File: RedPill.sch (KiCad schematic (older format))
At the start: 43 parts, among them J1 Conn_01x20, J2 Conn_01x20, J3 USB_C_Receptacle_USB2.0, J4 TagConnect_TC2030_SWD, J5 Conn_01x04, J6 Micro_SD_Card, SW1 SW_Push, U1 STM32F722RETx, U2 SRV05-4, U3 XC6206PxxxMR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

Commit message: Finish layout
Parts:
- added C?: 100nF, Capacitor_SMD:C_0402_1005Metric, symbol Device:C
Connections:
- net +3V3: now also C?.2
- net D+: now also U2.1 (IO1); no longer U2.3 (IO2)
- net D-: now also U2.3 (IO2); no longer U2.1 (IO1)
- net GND: now also C?.1
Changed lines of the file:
@@
 	1600 1350 1650 1350
 Wire Wire Line
-	1650 1350 1650 1400
-Wire Wire Line
 	1650 1450 1600 1450
 Wire Wire Line
 	1600 1550 1650 1550
-Wire Wire Line
-	1650 1550 1650 1600
 Wire Wire Line
 	1650 1650 1600 1650
@@
 Wire Wire Line
 	2050 1100 2050 1200
-Wire Wire Line
-	2250 1400 1650 1400
-Connection ~ 1650 1400
-Wire Wire Line
-	1650 1400 1650 1450
-Wire Wire Line
-	2250 1600 1650 1600
-Connection ~ 1650 1600
-Wire Wire Line
-	1650 1600 1650 1650
 NoConn ~ 1600 1950
 NoConn ~ 1600 2050
@@
 Text Label 1950 1400 0    50   ~ 0
 D-
-Text Label 1950 1600 0    50   ~ 0
+Text Label 1750 1600 0    50   ~ 0
 D+
 $Comp
@@
 	5100 3250 4950 3250
 Wire Wire Line
-	4950 3250 4950 2100
+	4950 3250 4950 2400
 $Comp
 L power:+3V3 #PWR0120
@@
 Wire Wire Line
 	2150 4550 5100 4550
+Wire Wire Line
+	1650 1350 1650 1400
+Wire Wire Line
+	1650 1550 1650 1600
+Wire Wire Line
+	1650 1600 2100 1600
+Wire Wire Line
+	2100 1600 2100 1400
+Wire Wire Line
+	2100 1400 2250 1400
+Connection ~ 1650 1600
+Wire Wire Line
+	1650 1600 1650 1650
+Wire Wire Line
+	1650 1400 2050 1400
+Wire Wire Line
+	2050 1400 2050 1500
+Wire Wire Line
+	2050 1500 2150 1500
+Wire Wire Line
+	2150 1500 2150 1600
+Wire Wire Line
+	2150 1600 2250 1600
+Connection ~ 1650 1400
+Wire Wire Line
+	1650 1400 1650 1450
+$Comp
+L Device:C C?
+U 1 1 604670F9
+P 4750 2400
+F 0 "C?" V 5002 2400 50  0000 C CNN
+F 1 "100nF" V 4911 2400 50  0000 C CNN
+F 2 "Capacitor_SMD:C_0402_1005Metric" H 4788 2250 50  0001 C CNN
+F 3 "https://datasheet.lcsc.com/szlcsc/Samsung-Electro-Mechanics-CL05B104KO5NNNC_C1525.pdf" H 4750 2400 50  0001 C CNN
+F 4 "C1525" H 4750 2400 50  0001 C CNN "LCSC"
+	1    4750 2400
+	0    -1   -1   0
+$EndComp
+$Comp
+L power:GND #PWR?
+U 1 1 604670FF
+P 4500 2450
+F 0 "#PWR?" H 4500 2200 50  0001 C CNN
+F 1 "GND" H 4505 2277 50  0000 C CNN
+F 2 "" H 4500 2450 50  0001 C CNN
+F 3 "" H 4500 2450 50  0001 C CNN
+	1    4500 2450
+	1    0    0    -1
+$EndComp
+Wire Wire Line
+	4500 2450 4500 2400
+Wire Wire Line
+	4600 2400 4500 2400
+Wire Wire Line
+	4900 2400 4950 2400
+Connection ~ 4950 2400
+Wire Wire Line
+	4950 2400 4950 2100
 $EndSCHEMATC

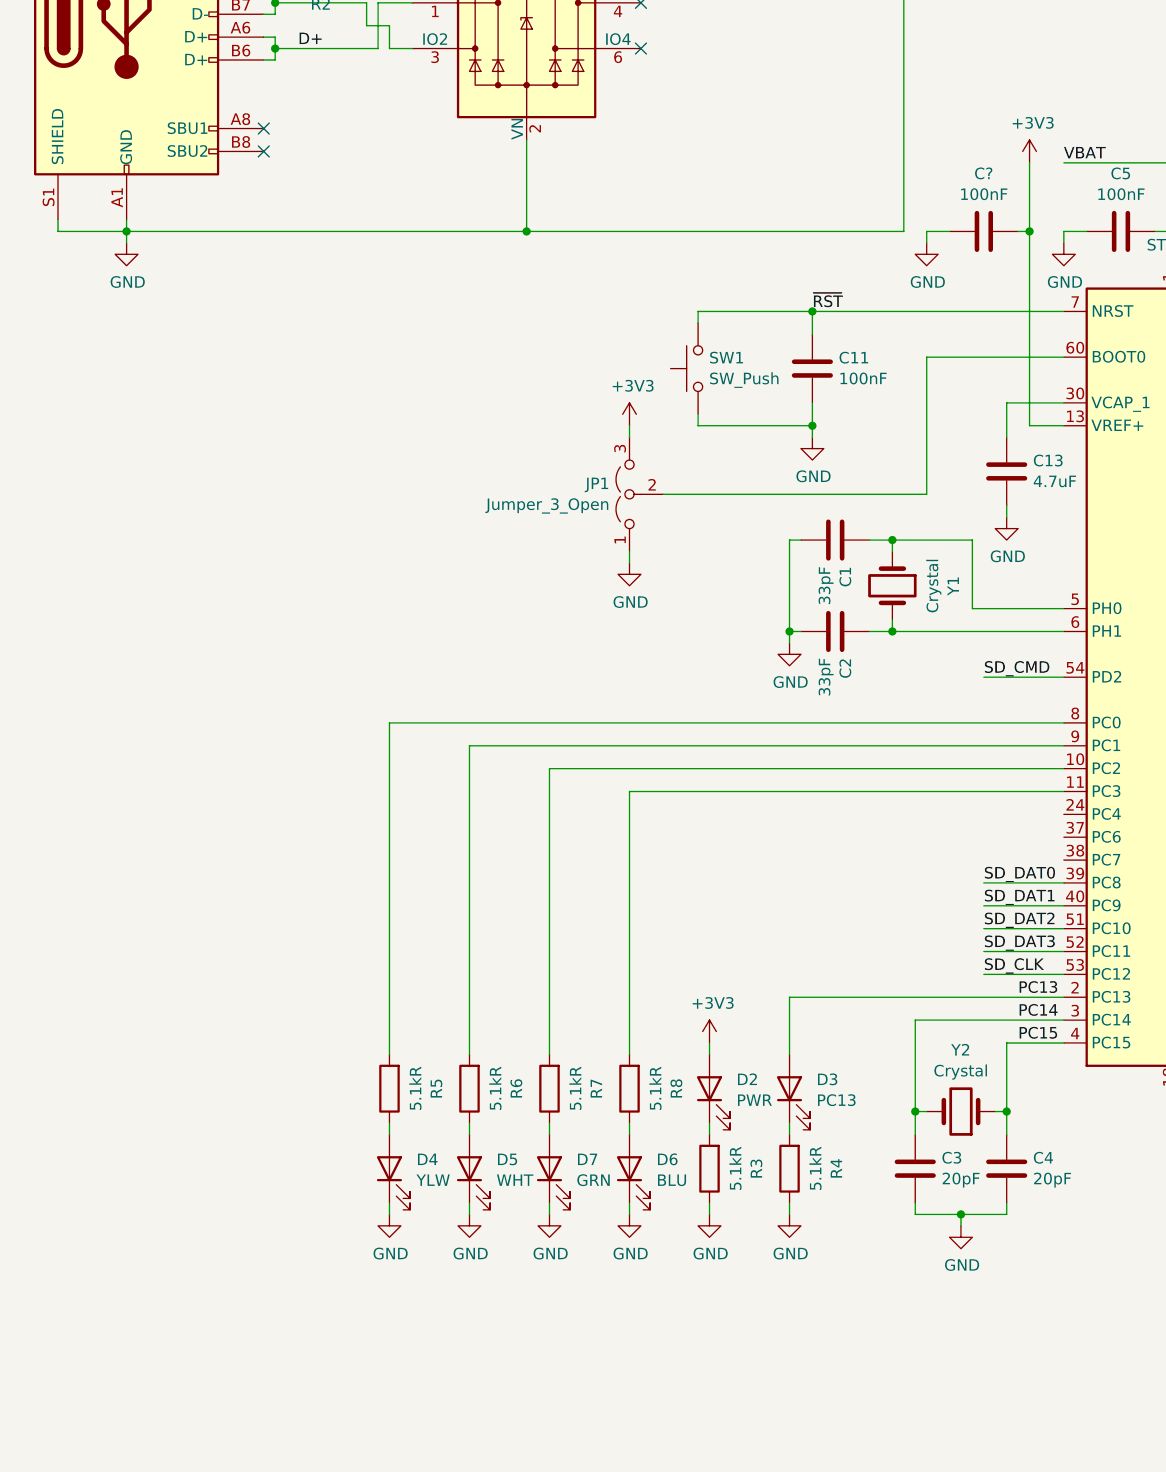
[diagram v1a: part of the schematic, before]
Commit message: Add JLCSMT tooling holes
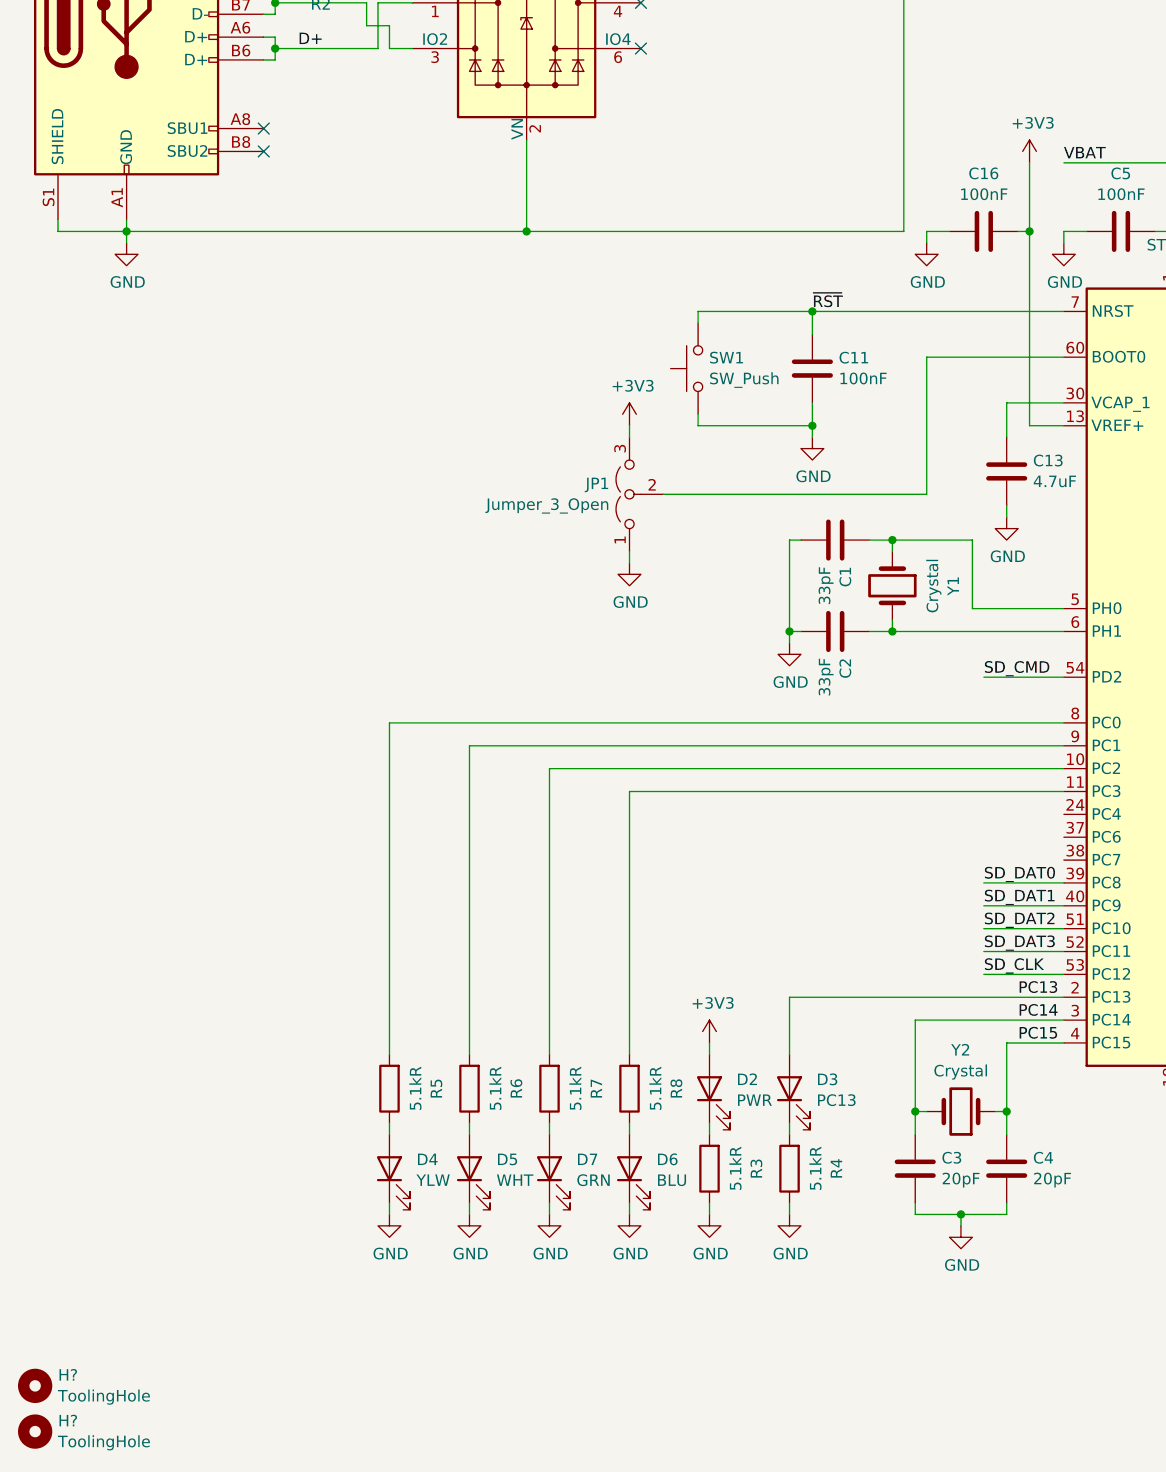
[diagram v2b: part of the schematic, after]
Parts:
- added H? (x2): ToolingHole, ToolingHole:ToolingHole_JLCSMT, symbol Mechanical:MountingHole
- gave numbers to parts that had none: 1
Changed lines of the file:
@@
 	1650 1400 1650 1450
 $Comp
-L Device:C C?
+L Device:C C16
 U 1 1 604670F9
 P 4750 2400
-F 0 "C?" V 5002 2400 50  0000 C CNN
+F 0 "C16" V 5002 2400 50  0000 C CNN
 F 1 "100nF" V 4911 2400 50  0000 C CNN
 F 2 "Capacitor_SMD:C_0402_1005Metric" H 4788 2250 50  0001 C CNN
@@
 $EndComp
 $Comp
-L power:GND #PWR?
+L power:GND #PWR0134
 U 1 1 604670FF
 P 4500 2450
-F 0 "#PWR?" H 4500 2200 50  0001 C CNN
+F 0 "#PWR0134" H 4500 2200 50  0001 C CNN
 F 1 "GND" H 4505 2277 50  0000 C CNN
 F 2 "" H 4500 2450 50  0001 C CNN
@@
 Wire Wire Line
 	4950 2400 4950 2100
+$Comp
+L Mechanical:MountingHole H?
+U 1 1 604A4294
+P 600 7650
+F 0 "H?" H 700 7696 50  0000 L CNN
+F 1 "ToolingHole" H 700 7605 50  0000 L CNN
+F 2 "ToolingHole:ToolingHole_JLCSMT" H 600 7650 50  0001 C CNN
+F 3 "~" H 600 7650 50  0001 C CNN
+	1    600  7650
+	1    0    0    -1
+$EndComp
+$Comp
+L Mechanical:MountingHole H?
+U 1 1 604A4906
+P 600 7450
+F 0 "H?" H 700 7496 50  0000 L CNN
+F 1 "ToolingHole" H 700 7405 50  0000 L CNN
+F 2 "ToolingHole:ToolingHole_JLCSMT" H 600 7450 50  0001 C CNN
+F 3 "~" H 600 7450 50  0001 C CNN
+	1    600  7450
+	1    0    0    -1
+$EndComp
 $EndSCHEMATC

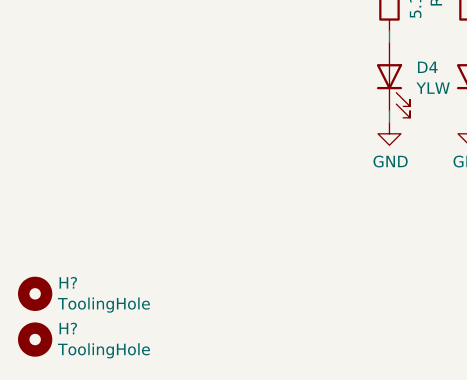
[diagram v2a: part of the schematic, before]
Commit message: Add silkscreen markings
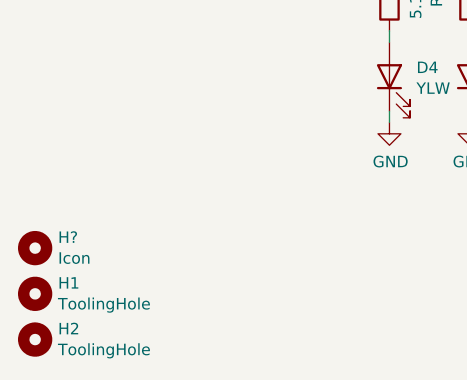
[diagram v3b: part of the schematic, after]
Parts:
- added H?: Icon, Icon:pill, symbol Mechanical:MountingHole
- gave numbers to parts that had none: 2
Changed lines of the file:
@@
 	4950 2400 4950 2100
 $Comp
-L Mechanical:MountingHole H?
+L Mechanical:MountingHole H2
 U 1 1 604A4294
 P 600 7650
-F 0 "H?" H 700 7696 50  0000 L CNN
+F 0 "H2" H 700 7696 50  0000 L CNN
 F 1 "ToolingHole" H 700 7605 50  0000 L CNN
 F 2 "ToolingHole:ToolingHole_JLCSMT" H 600 7650 50  0001 C CNN
@@
 $EndComp
 $Comp
-L Mechanical:MountingHole H?
+L Mechanical:MountingHole H1
 U 1 1 604A4906
 P 600 7450
-F 0 "H?" H 700 7496 50  0000 L CNN
+F 0 "H1" H 700 7496 50  0000 L CNN
 F 1 "ToolingHole" H 700 7405 50  0000 L CNN
 F 2 "ToolingHole:ToolingHole_JLCSMT" H 600 7450 50  0001 C CNN
@@
 	1    0    0    -1
 $EndComp
+$Comp
+L Mechanical:MountingHole H?
+U 1 1 604E4F2A
+P 600 7250
+F 0 "H?" H 700 7296 50  0000 L CNN
+F 1 "Icon" H 700 7205 50  0000 L CNN
+F 2 "Icon:pill" H 600 7250 50  0001 C CNN
+F 3 "~" H 600 7250 50  0001 C CNN
+	1    600  7250
+	1    0    0    -1
+$EndComp

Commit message: Add OSHW logo
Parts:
- added H?: OSHW, Symbol:OSHW-Symbol_6.7x6mm_SilkScreen, symbol Mechanical:MountingHole
- gave numbers to parts that had none: 1
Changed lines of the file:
@@
 $EndComp
 $Comp
-L Mechanical:MountingHole H?
+L Mechanical:MountingHole H3
 U 1 1 604E4F2A
 P 600 7250
-F 0 "H?" H 700 7296 50  0000 L CNN
+F 0 "H3" H 700 7296 50  0000 L CNN
 F 1 "Icon" H 700 7205 50  0000 L CNN
 F 2 "Icon:pill" H 600 7250 50  0001 C CNN
@@
 	1    0    0    -1
 $EndComp
+$Comp
+L Mechanical:MountingHole H?
+U 1 1 604EC694
+P 600 7050
+F 0 "H?" H 700 7096 50  0000 L CNN
+F 1 "OSHW" H 700 7005 50  0000 L CNN
+F 2 "Symbol:OSHW-Symbol_6.7x6mm_SilkScreen" H 600 7050 50  0001 C CNN
+F 3 "~" H 600 7050 50  0001 C CNN
+	1    600  7050
+	1    0    0    -1
+$EndComp

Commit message: Add LCSC partnumbers to all components
Yes, even ones JLC can not populate
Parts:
- J3: LCSC (none) -> C167321
- J6: LCSC (none) -> C266612
- gave numbers to parts that had none: 1
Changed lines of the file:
@@
 F 2 "Connector_USB:USB_C_Receptacle_Palconn_UTC16-G" H 1150 1450 50  0001 C CNN
 F 3 "https://www.usb.org/sites/default/files/documents/usb_type-c.zip" H 1150 1450 50  0001 C CNN
+F 4 "C167321" H 1000 1450 50  0001 C CNN "LCSC"
 	1    1000 1450
 	1    0    0    -1
@@
 F 2 "Connector_Card_MicroSD:XUNPU_TF.104" H 10500 5150 50  0001 C CNN
 F 3 "http://katalog.we-online.de/em/datasheet/693072010801.pdf" H 9350 4850 50  0001 C CNN
+F 4 "C266612" H 9350 4850 50  0001 C CNN "LCSC"
 	1    9350 4850
 	1    0    0    -1
@@
 $EndComp
 $Comp
-L Mechanical:MountingHole H?
+L Mechanical:MountingHole H4
 U 1 1 604EC694
 P 600 7050
-F 0 "H?" H 700 7096 50  0000 L CNN
+F 0 "H4" H 700 7096 50  0000 L CNN
 F 1 "OSHW" H 700 7005 50  0000 L CNN
 F 2 "Symbol:OSHW-Symbol_6.7x6mm_SilkScreen" H 600 7050 50  0001 C CNN
